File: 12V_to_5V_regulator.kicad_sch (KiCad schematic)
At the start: 10 parts, among them U4 TPS563201DDCR

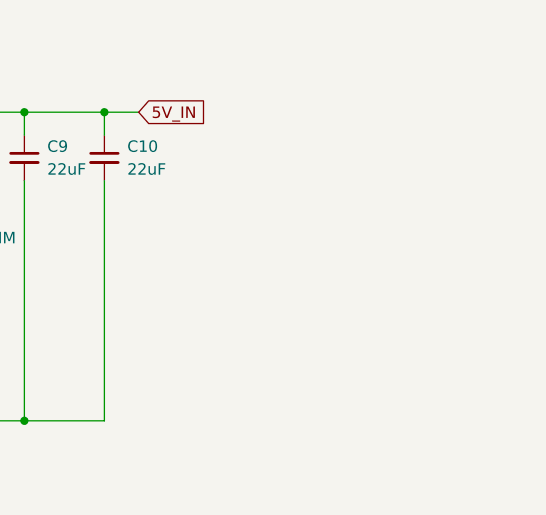
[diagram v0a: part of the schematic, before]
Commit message: updated components and nets
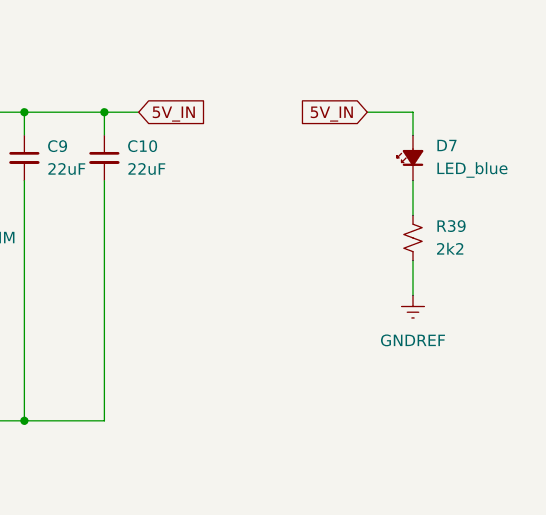
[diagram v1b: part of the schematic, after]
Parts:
- added D7: LED_blue, symbol Device:LED_Small_Filled
- added R39: 2k2, symbol Device:R_Small_US
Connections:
- net 5V_IN: now also D7.2 (A)
- net GNDREF: now also R39.2
- new net: D7.1 (K), R39.1
